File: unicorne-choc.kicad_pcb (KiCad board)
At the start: 2 copper layers, 293.4 x 118.8 mm, 175 parts, among them J1 Battery, J2 TPS43, J3 Expansion, J4 GPIO, J5 PAW3395 / PMW3360, J6 LED power in, Q1 AO3401A, Q2 2N7002, SW1 R0C0, SW10 R1C3, SW11 R1C4, SW12 R1C5, SW13 R2C0, SW14 R2C1, SW15 R2C2, SW16 R2C3, SW17 R2C4, SW18 R2C5, SW19 R0C6, SW2 R0C1, SW20 R1C6, SW21 R2C6, SW22 R3C0, SW23 R3C1, SW24 R3C2, SW25 R3C3, SW26 R3C4, SW27 R3C5, SW28 R4C0, SW29 R4C1, SW3 R0C2, SW30 R4C2, SW31 R4C3, SW32 R4C4, SW33 R4C5, SW34 R5C0, SW35 R5C1, SW36 R5C2, SW37 R5C3, SW38 R5C4, SW39 R5C5, SW4 R0C3, SW40 R3C6, SW41 R4C6, SW42 R5C6, SW43 Power, SW44 Reset, SW5 R0C4, SW6 R0C5, SW7 R1C0, SW8 R1C1, SW9 R1C2, U1 nice!nano v2, U2 SN74LV1T125

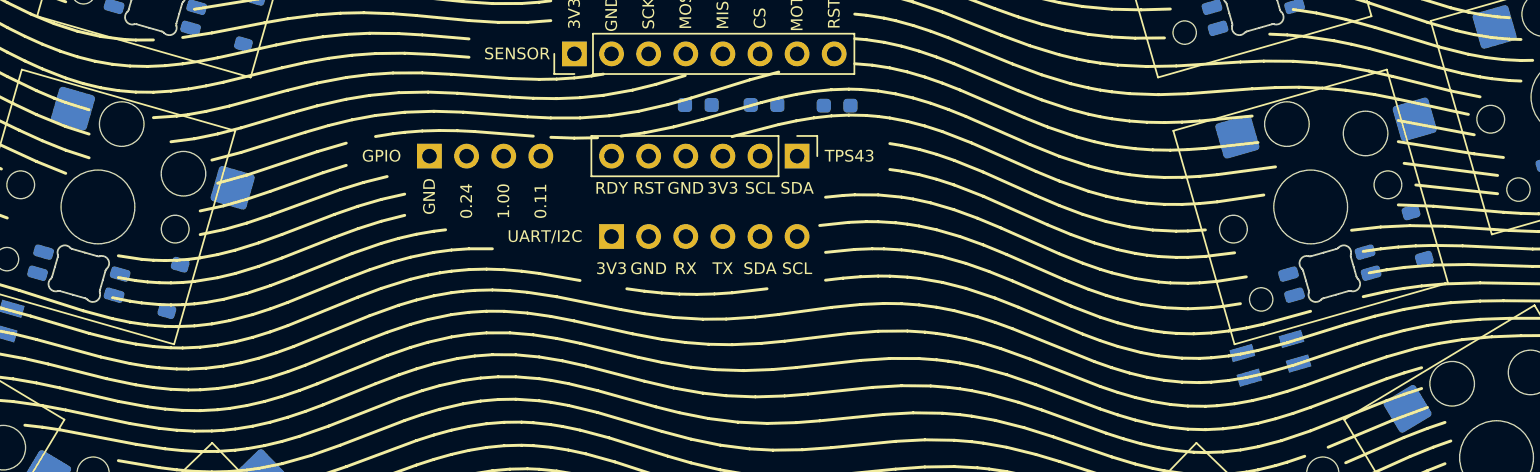
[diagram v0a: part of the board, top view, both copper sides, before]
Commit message: Fix the previous commit: gen_pcb.py had merge conflict markers
Restores tools/gen_pcb.py (and finish_route.py) to the current versions and
regenerates both unrouted boards with the reversed trackpad row and the
wider pad rows.

Co-Authored-By: Claude Opus 5.5 <noreply@anthropic.com>
Claude-Session: https://claude.ai/code/session_01D39ubfTYtq6FMvNmmbStTo
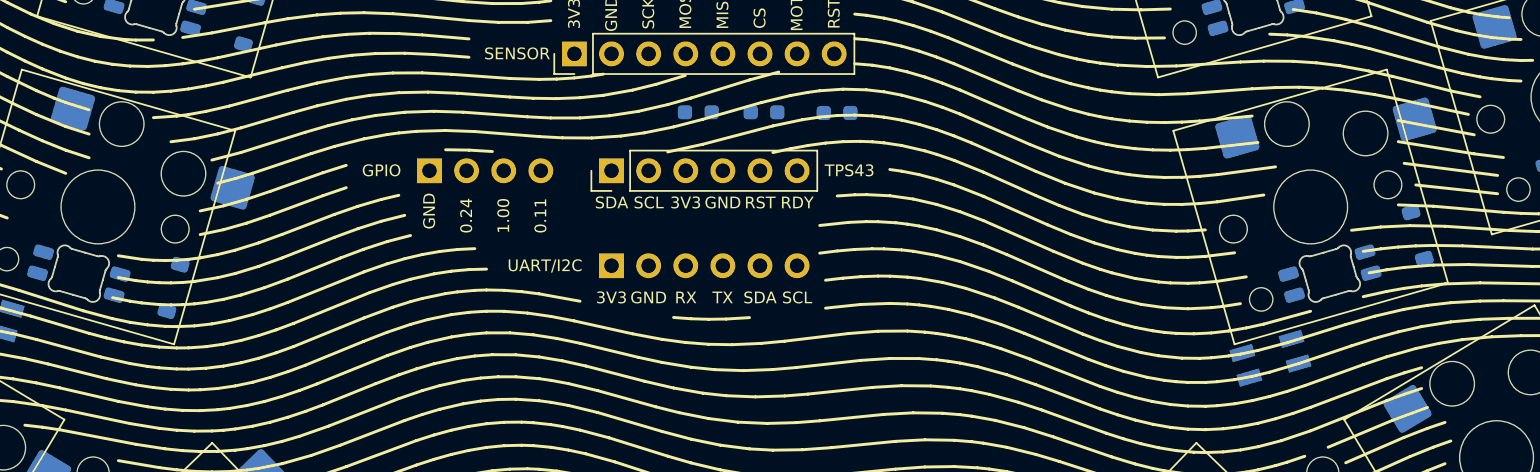
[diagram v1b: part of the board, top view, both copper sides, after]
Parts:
- moved J2 12.7 mm to (170.7, 101.0), turned to 90 degrees
- moved J3 2.00 mm to (170.7, 107.5)
- moved J4 1.00 mm to (158.2, 101.0)
- moved R3 0.50 mm to (176.6, 97.0)
- moved R4 0.50 mm to (181.1, 97.0)
- moved R5 0.50 mm to (186.1, 97.0)

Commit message: Heuristic branch: boards with only the fixed key-cell lanes
Both boards from gen_pcb.py with lanes.lay() applied and mounting holes moved
off the lanes; no maze routing or pours. MX: 504 tracks, 72 vias; Choc: 732
tracks, 168 vias; 208 connections left on each, no DRC errors.

Co-Authored-By: Claude Opus 5.5 <noreply@anthropic.com>
Claude-Session: https://claude.ai/code/session_01D39ubfTYtq6FMvNmmbStTo
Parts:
- moved H4 1.68 mm to (76.7, 58.8)
- moved H5 0.79 mm to (217.7, 73.6)
- moved H1 0.56 mm to (133.3, 70.3)
- moved H8 0.25 mm to (276.8, 59.1)
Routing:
- net LED_VDD: track 0.00 -> 673.5 mm
- net ROW1: track 0.00 -> 195.3 mm, vias 0 -> 16
- net ROW0: track 0.00 -> 195.3 mm, vias 0 -> 16
- net ROW4: track 0.00 -> 195.3 mm, vias 0 -> 16
- net ROW3: track 0.00 -> 195.3 mm, vias 0 -> 16
- net ROW2: track 0.00 -> 195.3 mm, vias 0 -> 16
- net ROW5: track 0.00 -> 195.3 mm, vias 0 -> 16
- net COL4: track 0.00 -> 87.4 mm, vias 0 -> 6
- net COL2: track 0.00 -> 87.4 mm, vias 0 -> 6
- net COL3: track 0.00 -> 87.4 mm, vias 0 -> 6
- net COL1: track 0.00 -> 87.4 mm, vias 0 -> 6
- net COL0: track 0.00 -> 87.4 mm, vias 0 -> 6
- net COL5: track 0.00 -> 87.4 mm, vias 0 -> 6
- net GND: track 0.00 -> 30.6 mm, vias 0 -> 36
- net /LEDs/LED_D12: track 0.00 -> 19.6 mm
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
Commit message: Heuristic branch on the current design, plus Quilter upload sets
Boards regenerated from the current tools: the picked LED order, wider tabs with
LED_VDD stacked under the row lane, no data lane through break-line tabs. Lanes
only (498 / 774 tracks on MX / Choc), 226 connections left, no DRC errors.

export/quilter/ (tools/quilter_export.py): for each board an as-is set and a
fallback set whose slots and LED cutouts are keepouts of the same shape, so
only the outer outline sits on Edge.Cuts. Waves left out.

Co-Authored-By: Claude Opus 5.5 <noreply@anthropic.com>
Claude-Session: https://claude.ai/code/session_01D39ubfTYtq6FMvNmmbStTo
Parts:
- LED1, LED2, LED3, LED43, LED44, LED46, LED48, LED5, LED6: value SK6812MINI -> SK6812MINI-E; footprint unicorne:LED_SK6812MINI_PLCC4_3.5x3.5mm_P1.75mm -> LED_SMD:LED_SK6812MINI-E_3.2x2.8mm_P1.5mm_ReverseMount
- LED11, LED13, LED18, LED23, LED26, LED29, LED37, LED40, LED8: value SK6812MINI-E -> SK6812MINI; footprint LED_SMD:LED_SK6812MINI-E_3.2x2.8mm_P1.5mm_ReverseMount -> unicorne:LED_SK6812MINI_PLCC4_3.5x3.5mm_P1.75mm
- moved LED30 85.7 mm to (207.6, 133.7), turned to -44 degrees
- moved LED46 83.2 mm to (288.3, 71.1), turned to 16 degrees
- moved LED31 77.2 mm to (233.7, 124.7), turned to 31 degrees
- moved LED10 71.2 mm to (60.5, 89.3)
- moved LED32 71.1 mm to (252.0, 116.7)
- moved LED45 69.9 mm to (259.4, 59.3)
- moved LED11 66.0 mm to (78.8, 74.5), turned to 164 degrees
- moved LED5 64.8 mm to (134.2, 108.0), turned to -16 degrees
- moved LED24 62.3 mm to (144.7, 71.5), turned to -16 degrees
- moved LED25 62.3 mm to (209.3, 71.5), turned to 16 degrees
- moved LED4 57.2 mm to (127.7, 110.8)
- moved LED16 57.0 mm to (85.3, 71.7)
- moved LED44 56.0 mm to (283.0, 52.8), turned to 16 degrees
- moved LED26 55.3 mm to (205.3, 77.3), turned to -164 degrees
- moved LED6 54.9 mm to (116.6, 100.5), turned to -16 degrees
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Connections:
- LED1 pad 1: /LEDs/LED_D1 -> GND
- LED1 pad 2: GND -> LED_DIN
- LED1 pad 3: LED_DIN -> LED_VDD
- LED1 pad 4: LED_VDD -> /LEDs/LED_D1
- LED11 pad 1: GND -> /LEDs/LED_D11
- LED11 pad 2: /LEDs/LED_D10 -> GND
- LED11 pad 3: LED_VDD -> /LEDs/LED_D10
- LED11 pad 4: /LEDs/LED_D11 -> LED_VDD
- LED13 pad 1: GND -> /LEDs/LED_D13
- LED13 pad 2: /LEDs/LED_D12 -> GND
- LED13 pad 3: LED_VDD -> /LEDs/LED_D12
- LED13 pad 4: /LEDs/LED_D13 -> LED_VDD
- LED18 pad 1: GND -> /LEDs/LED_D18
- LED18 pad 2: /LEDs/LED_D17 -> GND
- LED18 pad 3: LED_VDD -> /LEDs/LED_D17
- LED18 pad 4: /LEDs/LED_D18 -> LED_VDD
- LED2 pad 1: /LEDs/LED_D2 -> GND
- LED2 pad 2: GND -> /LEDs/LED_D1
- LED2 pad 3: /LEDs/LED_D1 -> LED_VDD
- LED2 pad 4: LED_VDD -> /LEDs/LED_D2
- LED23 pad 1: GND -> /LEDs/LED_D23
- LED23 pad 2: /LEDs/LED_D22 -> GND
- LED23 pad 3: LED_VDD -> /LEDs/LED_D22
- LED23 pad 4: /LEDs/LED_D23 -> LED_VDD
- LED26 pad 1: GND -> /LEDs/LED_D26
- LED26 pad 2: /LEDs/LED_D25 -> GND
- LED26 pad 3: LED_VDD -> /LEDs/LED_D25
- LED26 pad 4: /LEDs/LED_D26 -> LED_VDD
- LED29 pad 1: GND -> /LEDs/LED_D29
- LED29 pad 2: /LEDs/LED_D28 -> GND
- LED29 pad 3: LED_VDD -> /LEDs/LED_D28
- LED29 pad 4: /LEDs/LED_D29 -> LED_VDD
- LED3 pad 1: /LEDs/LED_D3 -> GND
- LED3 pad 2: GND -> /LEDs/LED_D2
- LED3 pad 3: /LEDs/LED_D2 -> LED_VDD
- LED3 pad 4: LED_VDD -> /LEDs/LED_D3
- LED37 pad 1: GND -> /LEDs/LED_D37
- LED37 pad 2: /LEDs/LED_D36 -> GND
- LED37 pad 3: LED_VDD -> /LEDs/LED_D36
- LED37 pad 4: /LEDs/LED_D37 -> LED_VDD
- LED40 pad 1: GND -> /LEDs/LED_D40
- LED40 pad 2: /LEDs/LED_D39 -> GND
- LED40 pad 3: LED_VDD -> /LEDs/LED_D39
- LED40 pad 4: /LEDs/LED_D40 -> LED_VDD
- LED43 pad 1: /LEDs/LED_D43 -> GND
- LED43 pad 2: GND -> /LEDs/LED_D42
- LED43 pad 3: /LEDs/LED_D42 -> LED_VDD
- LED43 pad 4: LED_VDD -> /LEDs/LED_D43
- LED44 pad 1: /LEDs/LED_D44 -> GND
- LED44 pad 2: GND -> /LEDs/LED_D43
- LED44 pad 3: /LEDs/LED_D43 -> LED_VDD
- LED44 pad 4: LED_VDD -> /LEDs/LED_D44
- LED46 pad 1: /LEDs/LED_D46 -> GND
- LED46 pad 2: GND -> /LEDs/LED_D45
- LED46 pad 3: /LEDs/LED_D45 -> LED_VDD
- LED46 pad 4: LED_VDD -> /LEDs/LED_D46
- LED48 pad 1: /LEDs/LED_D48 -> GND
- LED48 pad 2: GND -> /LEDs/LED_D47
- LED48 pad 3: /LEDs/LED_D47 -> LED_VDD
- LED48 pad 4: LED_VDD -> /LEDs/LED_D48
- LED5 pad 1: /LEDs/LED_D5 -> GND
- LED5 pad 2: GND -> /LEDs/LED_D4
- LED5 pad 3: /LEDs/LED_D4 -> LED_VDD
- LED5 pad 4: LED_VDD -> /LEDs/LED_D5
- LED6 pad 1: /LEDs/LED_D6 -> GND
- LED6 pad 2: GND -> /LEDs/LED_D5
- LED6 pad 3: /LEDs/LED_D5 -> LED_VDD
- LED6 pad 4: LED_VDD -> /LEDs/LED_D6
- LED8 pad 1: GND -> /LEDs/LED_D8
- LED8 pad 2: /LEDs/LED_D7 -> GND
- LED8 pad 3: LED_VDD -> /LEDs/LED_D7
- LED8 pad 4: /LEDs/LED_D8 -> LED_VDD
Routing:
- net /LEDs/LED_D12: track 19.6 -> 0.00 mm
- net /LEDs/LED_D7: track 19.6 -> 0.00 mm
- net /LEDs/LED_D17: track 19.6 -> 0.00 mm
- net /LEDs/LED_D31: track 19.6 -> 0.00 mm
- net /LEDs/LED_D43: track 0.00 -> 19.6 mm
- net /LEDs/LED_D41: track 19.6 -> 0.00 mm
- net /LEDs/LED_D36: track 19.6 -> 0.00 mm
- net /LEDs/LED_D21: track 0.00 -> 17.6 mm
- net /LEDs/LED_D15: track 17.6 -> 0.00 mm
- net /LEDs/LED_D10: track 17.6 -> 0.00 mm
- net /LEDs/LED_D33: track 17.6 -> 0.00 mm
- net /LEDs/LED_D28: track 17.6 -> 0.00 mm
- net /LEDs/LED_D18: track 17.6 -> 0.00 mm
- net /LEDs/LED_D8: track 17.6 -> 0.00 mm
- net /LEDs/LED_D16: track 0.00 -> 17.6 mm
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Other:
- outline, holes or cut-outs redrawn
